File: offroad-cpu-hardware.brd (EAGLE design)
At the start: 78.7 x 25.4 mm, 15 parts, among them IC1 ATmega328-DIP-Prgrammed, Q1 2N3904, U1 LCD-16X2NOHOLES, Y1 16MHz

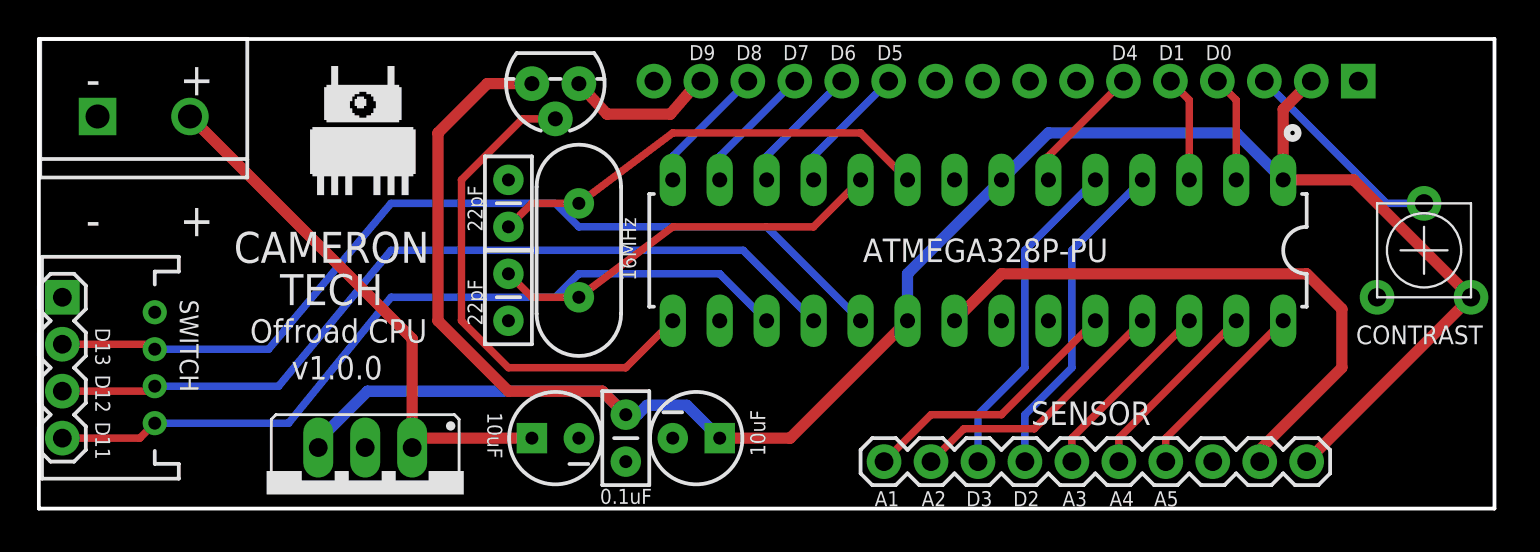
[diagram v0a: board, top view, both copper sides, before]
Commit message: Removes timing crystal and associated capacitors
http://arduino.cc/en/Tutorial/ArduinoToBreadboard
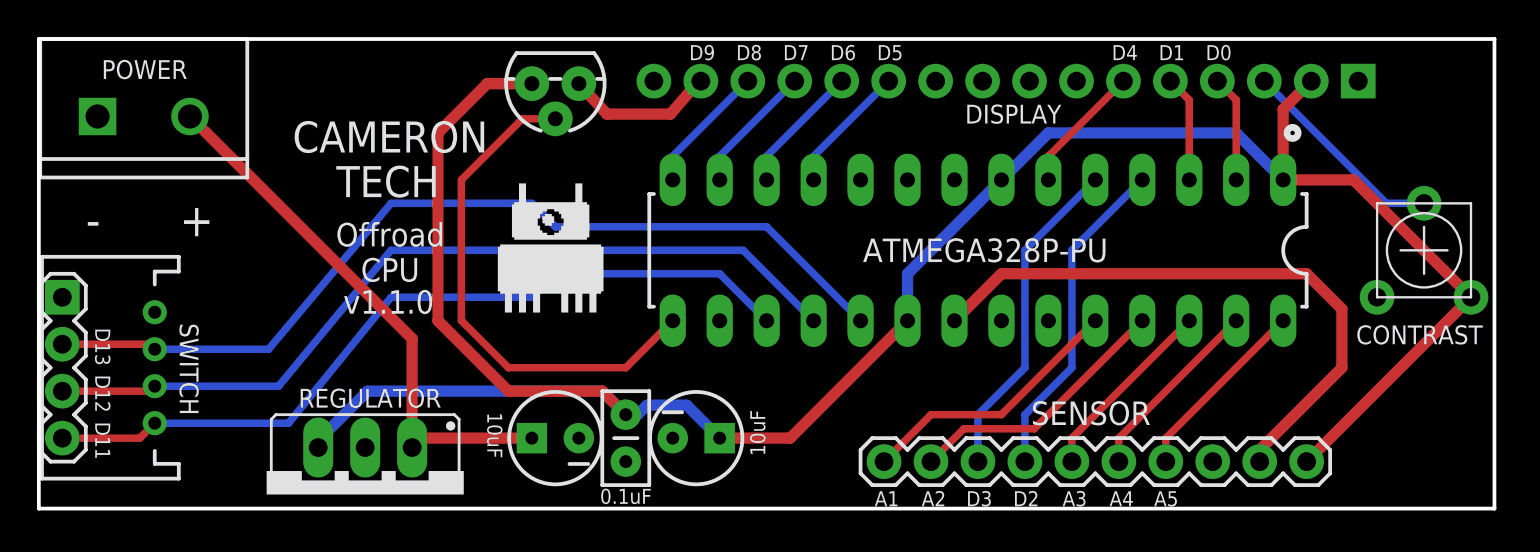
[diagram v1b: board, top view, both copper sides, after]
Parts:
- removed C1, C2: 22pF, SparkFun:CAP-PTH-SMALL2
- removed Y1: 16MHz, SparkFun:HC49US
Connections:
- removed net XTAL1: C2.1, IC1.9, Y1.2
- removed net XTAL2: C1.1, IC1.10, Y1.1
- net GND: no longer C1.2, C2.2
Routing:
- net XTAL1: track 24.4 -> 0.00 mm
- net XTAL2: track 21.9 -> 0.00 mm
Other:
- board text added: "DISPLAY"
- board text added: "POWER"
- board text added: "REGULATOR"
- board text added: "http://camte.ch/offroad-cpu"
- board text added: "v1.1.0"
- board text removed: "16MHz"
- board text removed: "22pF"
- board text removed: "http://git.io/offroadcpu"
- board text removed: "v1.0.0"
